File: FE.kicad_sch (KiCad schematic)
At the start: 33 parts, among them Q3 DMN62D0UW, Q4 DMN62D0UW, U14 REF2025, U15 OPA140AIDBVR, U19 MCP4452-104E, U2 MCP4728

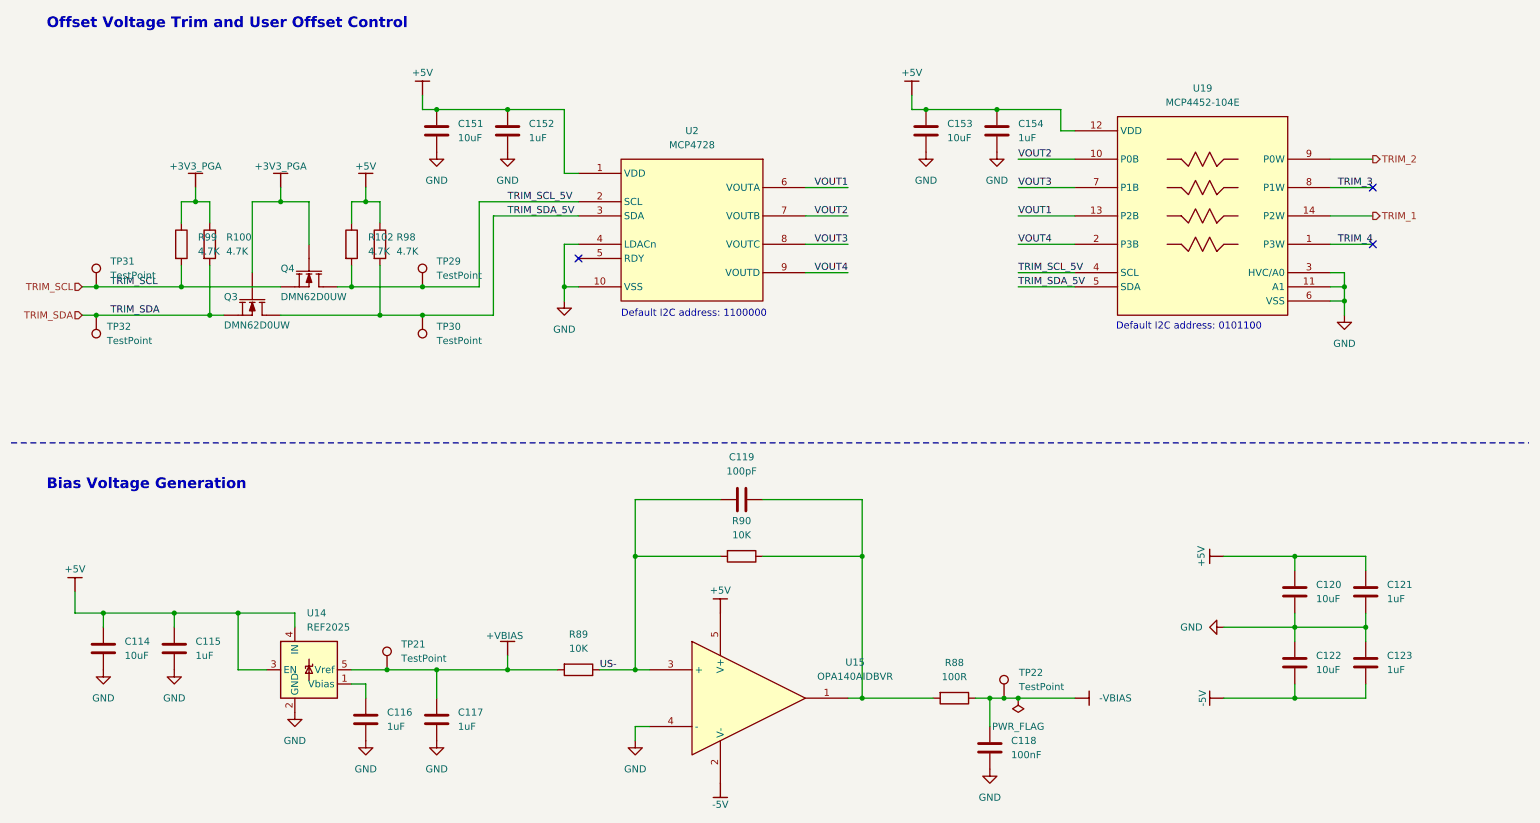
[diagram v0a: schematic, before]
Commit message: decided on clk source and MCU
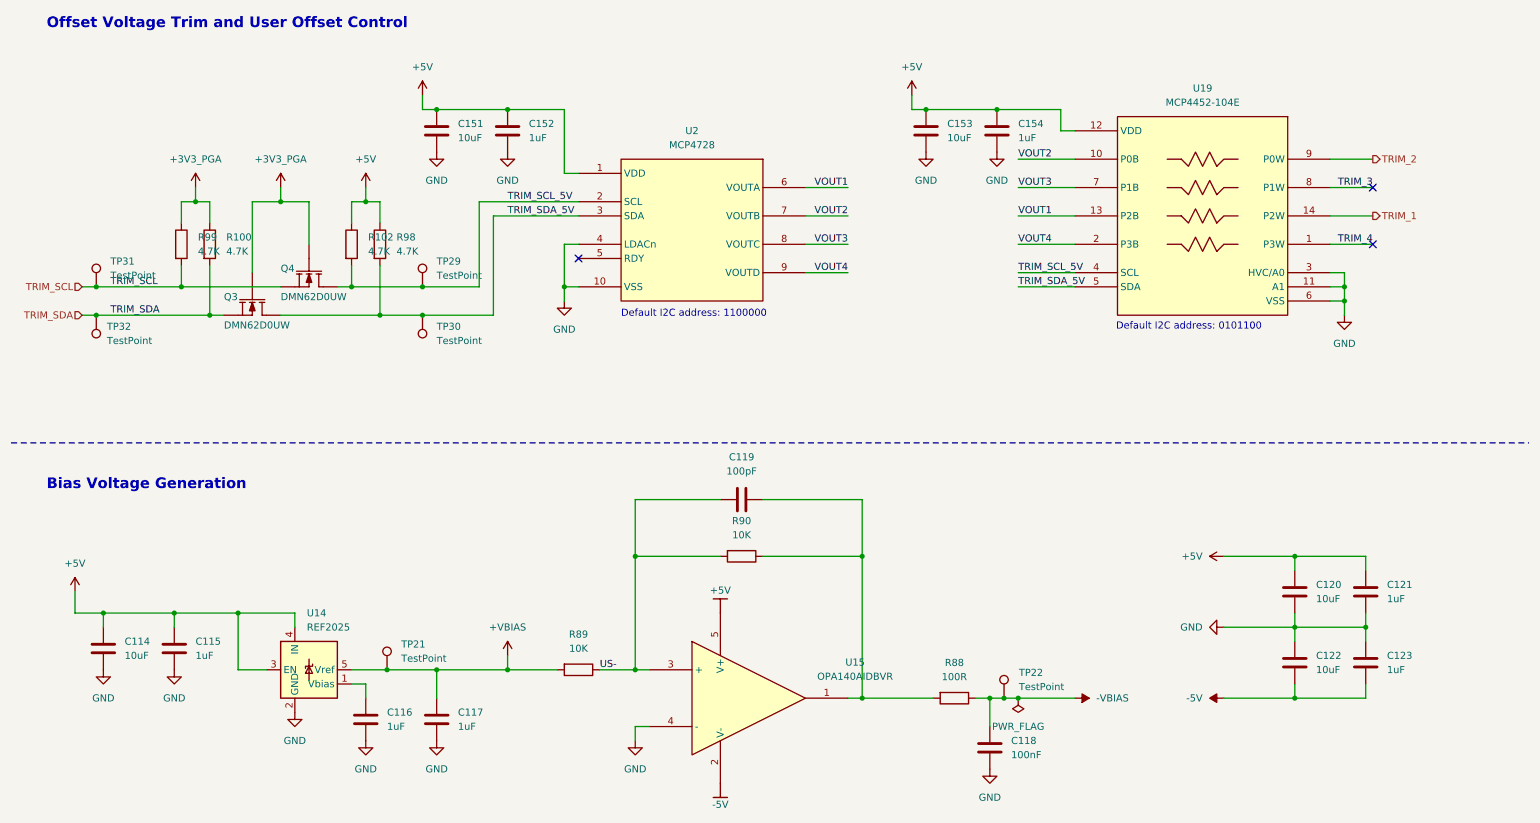
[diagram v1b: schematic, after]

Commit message: schematic complete. no ERC errors
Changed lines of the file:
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@@
 	)
 	(junction
+		(at 88.9 135.89)
+		(diameter 0)
+		(color 0 0 0 0)
+	)
+	(junction
 		(at 251.46 67.31)
 		(diameter 0)
@@
 	)
 	(junction
+		(at 194.31 140.97)
+		(diameter 0)
+		(color 0 0 0 0)
+	)
+	(junction
 		(at 43.18 67.31)
 		(diameter 0)
@@
 	)
 	(junction
-		(at 193.04 140.97)
-		(diameter 0)
-		(color 0 0 0 0)
-	)
-	(junction
 		(at 255.27 128.27)
 		(diameter 0)
@@
 	)
 	(junction
-		(at 101.6 135.89)
-		(diameter 0)
-		(color 0 0 0 0)
-	)
-	(junction
-		(at 88.9 135.89)
-		(diameter 0)
-		(color 0 0 0 0)
-	)
-	(junction
 		(at 27.94 67.31)
 		(diameter 0)
@@
 	(wire
 		(pts
-			(xy 101.6 133.35) (xy 101.6 135.89)
+			(xy 165.1 105.41) (xy 165.1 115.57)
 		)
 		(stroke
@@
 	(wire
 		(pts
-			(xy 165.1 105.41) (xy 165.1 115.57)
+			(xy 43.18 52.07) (xy 43.18 55.88)
 		)
 		(stroke
@@
 	(wire
 		(pts
-			(xy 43.18 52.07) (xy 43.18 55.88)
+			(xy 251.46 72.39) (xy 251.46 69.85)
 		)
 		(stroke
@@
 	(wire
 		(pts
-			(xy 251.46 72.39) (xy 251.46 69.85)
+			(xy 29.21 125.73) (xy 41.91 125.73)
 		)
 		(stroke
@@
 	(wire
 		(pts
-			(xy 29.21 125.73) (xy 41.91 125.73)
+			(xy 154.94 64.77) (xy 162.56 64.77)
 		)
 		(stroke
@@
 	(wire
 		(pts
-			(xy 154.94 64.77) (xy 162.56 64.77)
+			(xy 88.9 135.89) (xy 110.49 135.89)
+		)
+		(stroke
+			(width 0)
+			(type default)
+		)
+	)
+	(wire
+		(pts
+			(xy 194.31 140.97) (xy 203.2 140.97)
 		)
 		(stroke
@@
 	(wire
 		(pts
-			(xy 190.5 140.97) (xy 193.04 140.97)
-		)
-		(stroke
-			(width 0)
-			(type default)
-		)
-	)
-	(wire
-		(pts
 			(xy 60.96 72.39) (xy 78.74 72.39)
 		)
@@
 	(wire
 		(pts
-			(xy 203.2 140.97) (xy 193.04 140.97)
+			(xy 190.5 140.97) (xy 194.31 140.97)
 		)
 		(stroke
@@
 	(wire
 		(pts
-			(xy 88.9 135.89) (xy 101.6 135.89)
-		)
-		(stroke
-			(width 0)
-			(type default)
-		)
-	)
-	(wire
-		(pts
-			(xy 101.6 135.89) (xy 110.49 135.89)
-		)
-		(stroke
-			(width 0)
-			(type default)
-		)
-	)
-	(wire
-		(pts
 			(xy 200.66 35.56) (xy 200.66 39.37)
 		)
@@
 		)
 	)
+	(label "+VBIAS"
+		(at 99.06 135.89 0)
+		(effects
+			(font
+				(size 1.27 1.27)
+			)
+			(justify left bottom)
+		)
+	)
 	(label "VOUT1"
 		(at 162.56 49.53 180)
@@
 	)
 	(symbol
-		(lib_id "power:PWR_FLAG")
-		(at 193.04 140.97 180)
-		(unit 1)
-		(exclude_from_sim no)
-		(in_bom yes)
-		(on_board yes)
-		(dnp no)
-		(fields_autoplaced yes)
-		(property "Reference" "#FLG06"
-			(at 193.04 142.875 0)
-			(effects
-				(font
-					(size 1.27 1.27)
-				)
-				(hide yes)
-			)
-		)
-		(property "Value" "PWR_FLAG"
-			(at 193.04 146.05 0)
-			(effects
-				(font
-					(size 1.27 1.27)
-				)
-			)
-		)
-		(property "Footprint" ""
-			(at 193.04 140.97 0)
-			(effects
-				(font
-					(size 1.27 1.27)
-				)
-				(hide yes)
-			)
-		)
-		(property "Datasheet" "~"
-			(at 193.04 140.97 0)
-			(effects
-				(font
-					(size 1.27 1.27)
-				)
-				(hide yes)
-			)
-		)
-		(property "Description" "Special symbol for telling ERC where power comes from"
-			(at 193.04 140.97 0)
-			(effects
-				(font
-					(size 1.27 1.27)
-				)
-				(hide yes)
-			)
-		)
-		(pin "1"
-		)
-		(instances
-			(project "thunderscope-lite"
-				(path "/920a8b65-6ec2-414c-bfee-6322de42233d/a8bce2c4-277d-41bd-bb7b-cc0ae9ebe2d6"
-					(reference "#FLG06")
-					(unit 1)
-				)
-			)
-		)
-	)
-	(symbol
 		(lib_id "Device:R")
 		(at 114.3 135.89 270)
@@
 	)
 	(symbol
+		(lib_id "power:PWR_FLAG")
+		(at 124.46 135.89 180)
+		(unit 1)
+		(exclude_from_sim no)
+		(in_bom yes)
+		(on_board yes)
+		(dnp no)
+		(fields_autoplaced yes)
+		(property "Reference" "#FLG014"
+			(at 124.46 137.795 0)
+			(effects
+				(font
+					(size 1.27 1.27)
+				)
+				(hide yes)
+			)
+		)
+		(property "Value" "PWR_FLAG"
+			(at 124.46 140.97 0)
+			(effects
+				(font
+					(size 1.27 1.27)
+				)
+			)
+		)
+		(property "Footprint" ""
+			(at 124.46 135.89 0)
+			(effects
+				(font
+					(size 1.27 1.27)
+				)
+				(hide yes)
+			)
+		)
+		(property "Datasheet" "~"
+			(at 124.46 135.89 0)
+			(effects
+				(font
+					(size 1.27 1.27)
+				)
+				(hide yes)
+			)
+		)
+		(property "Description" "Special symbol for telling ERC where power comes from"
+			(at 124.46 135.89 0)
+			(effects
+				(font
+					(size 1.27 1.27)
+				)
+				(hide yes)
+			)
+		)
+		(pin "1"
+		)
+		(instances
+			(project "thunderscope-lite"
+				(path "/920a8b65-6ec2-414c-bfee-6322de42233d/a8bce2c4-277d-41bd-bb7b-cc0ae9ebe2d6"
+					(reference "#FLG014")
+					(unit 1)
+				)
+			)
+		)
+	)
+	(symbol
 		(lib_id "Device:R")
 		(at 181.61 140.97 270)
@@
 	)
 	(symbol
+		(lib_id "power:PWR_FLAG")
+		(at 194.31 140.97 180)
+		(unit 1)
+		(exclude_from_sim no)
+		(in_bom yes)
+		(on_board yes)
+		(dnp no)
+		(fields_autoplaced yes)
+		(property "Reference" "#FLG06"
+			(at 194.31 142.875 0)
+			(effects
+				(font
+					(size 1.27 1.27)
+				)
+				(hide yes)
+			)
+		)
+		(property "Value" "PWR_FLAG"
+			(at 194.31 146.05 0)
+			(effects
+				(font
+					(size 1.27 1.27)
+				)
+			)
+		)
+		(property "Footprint" ""
+			(at 194.31 140.97 0)
+			(effects
+				(font
+					(size 1.27 1.27)
+				)
+				(hide yes)
+			)
+		)
+		(property "Datasheet" "~"
+			(at 194.31 140.97 0)
+			(effects
+				(font
+					(size 1.27 1.27)
+				)
+				(hide yes)
+			)
+		)
+		(property "Description" "Special symbol for telling ERC where power comes from"
+			(at 194.31 140.97 0)
+			(effects
+				(font
+					(size 1.27 1.27)
+				)
+				(hide yes)
+			)
+		)
+		(pin "1"
+		)
+		(instances
+			(project "thunderscope-lite"
+				(path "/920a8b65-6ec2-414c-bfee-6322de42233d/a8bce2c4-277d-41bd-bb7b-cc0ae9ebe2d6"
+					(reference "#FLG06")
+					(unit 1)
+				)
+			)
+		)
+	)
+	(symbol
 		(lib_id "Thunderscope_Rev5:IC DAC QUAD MCP4728")
 		(at 134.62 57.15 0)
@@
 					(unit 1)
 				)
-			)
-		)
-	)
-	(symbol
-		(lib_id "power:VDD")
-		(at 101.6 133.35 0)
-		(unit 1)
-		(exclude_from_sim no)
-		(in_bom yes)
-		(on_board yes)
-		(dnp no)
-		(fields_autoplaced yes)
-		(property "Reference" "#PWR0205"
-			(at 101.6 137.16 0)
-			(effects
-				(font
-					(size 1.27 1.27)
-				)
-				(hide yes)
-			)
-		)
-		(property "Value" "+VBIAS"
-			(at 101.6 128.27 0)
-			(effects
-				(font
-					(size 1.27 1.27)
-				)
-			)
-		)
-		(property "Footprint" ""
-			(at 101.6 133.35 0)
-			(effects
-				(font
-					(size 1.27 1.27)
-				)
-				(hide yes)
-			)
-		)
-		(property "Datasheet" ""
-			(at 101.6 133.35 0)
-			(effects
-				(font
-					(size 1.27 1.27)
-				)
-				(hide yes)
-			)
-		)
-		(property "Description" "Power symbol creates a global label with name \"VDD\""
-			(at 101.6 133.35 0)
-			(effects
-				(font
-					(size 1.27 1.27)
-				)
-				(hide yes)
-			)
-		)
-		(pin "1"
-		)
-		(instances
-			(project "thunderscope-lite"
-				(path "/920a8b65-6ec2-414c-bfee-6322de42233d/a8bce2c4-277d-41bd-bb7b-cc0ae9ebe2d6"
-					(reference "#PWR0205")
-					(unit 1)
-				)
